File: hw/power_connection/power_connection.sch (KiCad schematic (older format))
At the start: 18 parts

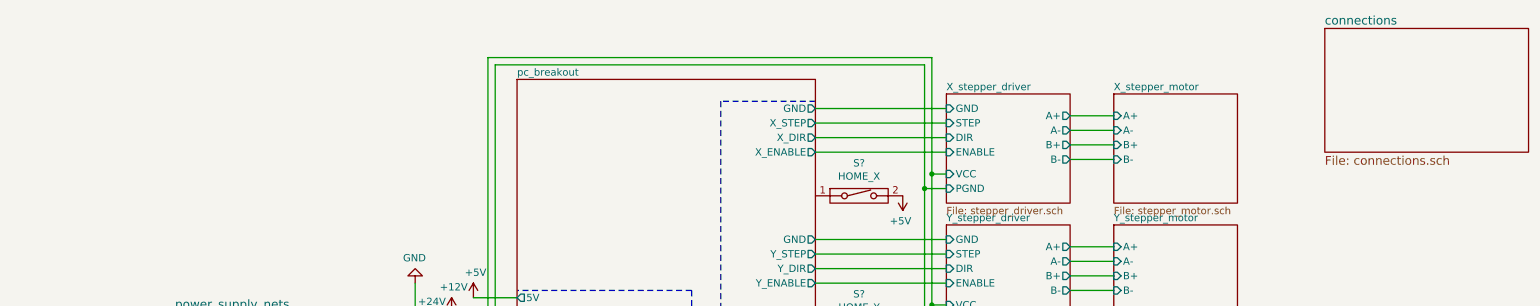
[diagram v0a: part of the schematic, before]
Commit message: Adjust track width in stepper breakout
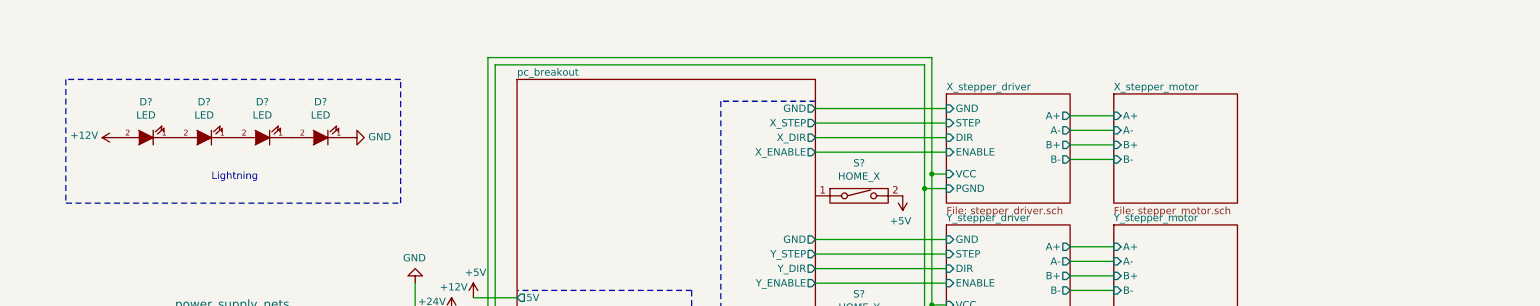
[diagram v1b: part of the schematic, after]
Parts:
- added D? (x4): LED, symbol LED
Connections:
- net +12V: now also D?.2 (A)
- net GND: now also D?.1 (K)
- new net: D?.1 (K), D?.2 (A) (x3)
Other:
- note added: "Lightning"
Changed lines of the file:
@@
 $EndDescr
-$Sheet
-S 9700 500  1400 850
-U 57A7F9AD
-F0 "connections" 60
-F1 "connections.sch" 60
-$EndSheet
 $Sheet
 S 1800 2450 1600 1550
@@
 	7000 5850 7000 5600
 Connection ~ 7000 5600
+$Comp
+L LED D?
+U 1 1 57D5B138
+P 1600 1250
+F 0 "D?" H 1600 1005 50  0000 C CNN
+F 1 "LED" H 1600 1096 50  0000 C CNN
+F 2 "" H 1600 1250 50  0000 C CNN
+F 3 "" H 1600 1250 50  0000 C CNN
+	1    1600 1250
+	-1   0    0    1
+$EndComp
+$Comp
+L LED D?
+U 1 1 57D5B8C3
+P 2000 1250
+F 0 "D?" H 2000 1005 50  0000 C CNN
+F 1 "LED" H 2000 1096 50  0000 C CNN
+F 2 "" H 2000 1250 50  0000 C CNN
+F 3 "" H 2000 1250 50  0000 C CNN
+	1    2000 1250
+	-1   0    0    1
+$EndComp
+$Comp
+L LED D?
+U 1 1 57D5BCAF
+P 2400 1250
+F 0 "D?" H 2400 1005 50  0000 C CNN
+F 1 "LED" H 2400 1096 50  0000 C CNN
+F 2 "" H 2400 1250 50  0000 C CNN
+F 3 "" H 2400 1250 50  0000 C CNN
+	1    2400 1250
+	-1   0    0    1
+$EndComp
+$Comp
+L LED D?
+U 1 1 57D5C08E
+P 2800 1250
+F 0 "D?" H 2800 1005 50  0000 C CNN
+F 1 "LED" H 2800 1096 50  0000 C CNN
+F 2 "" H 2800 1250 50  0000 C CNN
+F 3 "" H 2800 1250 50  0000 C CNN
+	1    2800 1250
+	-1   0    0    1
+$EndComp
+$Comp
+L GND #PWR?
+U 1 1 57D5C476
+P 3000 1250
+F 0 "#PWR?" H 3000 1000 50  0001 C CNN
+F 1 "GND" V 3005 1122 50  0000 R CNN
+F 2 "" H 3000 1250 50  0000 C CNN
+F 3 "" H 3000 1250 50  0000 C CNN
+	1    3000 1250
+	0    -1   -1   0
+$EndComp
+$Comp
+L +12V #PWR?
+U 1 1 57D5D186
+P 1400 1250
+F 0 "#PWR?" H 1400 1100 50  0001 C CNN
+F 1 "+12V" V 1415 1378 50  0000 L CNN
+F 2 "" H 1400 1250 50  0000 C CNN
+F 3 "" H 1400 1250 50  0000 C CNN
+	1    1400 1250
+	0    -1   -1   0
+$EndComp
+Wire Notes Line
+	1050 850  1050 1700
+Wire Notes Line
+	1050 1700 3350 1700
+Wire Notes Line
+	3350 1700 3350 850
+Wire Notes Line
+	3350 850  1050 850
+Text Notes 2050 1550 0    50   ~ 0
+Lightning
 $EndSCHEMATC
